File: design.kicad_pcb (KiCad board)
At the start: 4 copper layers, 64 x 34 mm, 30 parts, among them J1 Conn_01x03

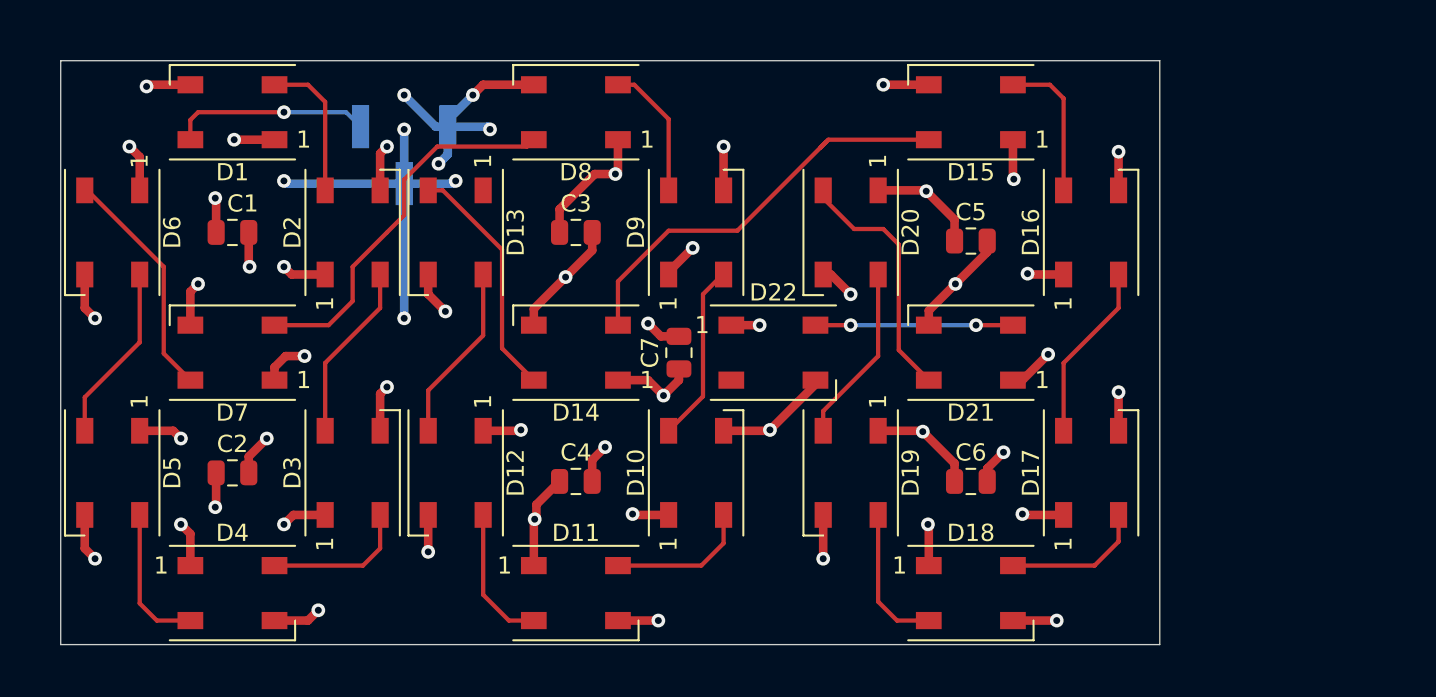
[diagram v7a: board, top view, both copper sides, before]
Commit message: PCB: make edgecut bigger
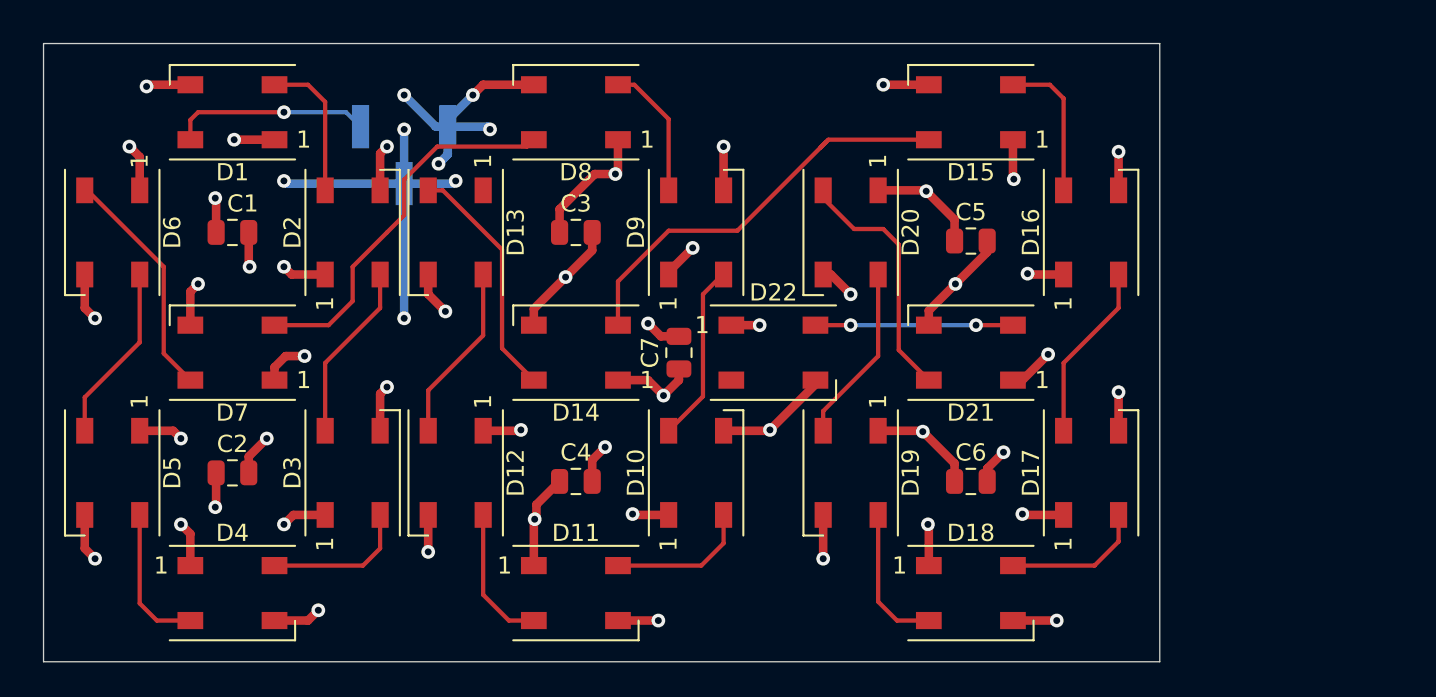
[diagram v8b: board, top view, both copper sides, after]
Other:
- board size 64 x 34 mm -> 65 x 36 mm
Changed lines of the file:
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@@
   (gr_line (start 85 87) (end 151 87) (layer Dwgs.User) (width 0.15))
   (gr_line (start 87 73) (end 151 73) (layer Dwgs.User) (width 0.15))
-  (gr_line (start 151 104) (end 87 104) (layer Edge.Cuts) (width 0.05))
-  (gr_line (start 151 70) (end 151 104) (layer Edge.Cuts) (width 0.05))
-  (gr_line (start 87 70) (end 151 70) (layer Edge.Cuts) (width 0.05))
-  (gr_line (start 87 104) (end 87 70) (layer Edge.Cuts) (width 0.05))
+  (gr_line (start 151 105) (end 86 105) (layer Edge.Cuts) (width 0.05))
+  (gr_line (start 151 69) (end 151 105) (layer Edge.Cuts) (width 0.05))
+  (gr_line (start 86 69) (end 151 69) (layer Edge.Cuts) (width 0.05))
+  (gr_line (start 86 105) (end 86 69) (layer Edge.Cuts) (width 0.05))
   (dimension 34 (width 0.15) (layer Dwgs.User)
     (gr_text "34.000 mm" (at 73.7 87 270) (layer Dwgs.User)
